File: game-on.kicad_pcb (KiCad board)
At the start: 2 copper layers, 125 x 70 mm, 339 parts, among them J1 USB_C, J2 Qwiic, J3 DEBUG, Q1 CJ2302, Q2 CJ2305, Q3 BC817, SW1 POWER, SW2 A, SW3 B, SW4 X, SW5 Y, SW6 RESET, SW7 BOOT, U1 HX9193-33GB, U2 QX2304, U3 ST7735S-SPI-14pin, U4 W25QXX128MBIT, U5 RP2040, X1 #badgelife, Y1 12MHz

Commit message: Tweaked a few values
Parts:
- C15, C16: value 15pF -> 30pF
- R13, R14: value 27 -> 27R
- R6: value 22R -> 27R
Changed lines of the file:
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@@
     (property "Sheetname" "Buttons")
     (attr through_hole)
-    (fp_text reference "SW2" (at 0 0.5 150) (layer "F.SilkS")
+    (fp_text reference "SW2" (at 0 0.5 150) (layer "F.SilkS") hide
       (effects (font (size 1 1) (thickness 0.15)))
     )
@@
     (property "Sheetname" "Buttons")
     (attr through_hole)
-    (fp_text reference "SW5" (at 0 0.5 60) (layer "F.SilkS")
+    (fp_text reference "SW5" (at 0 0.5 60) (layer "F.SilkS") hide
       (effects (font (size 1 1) (thickness 0.15)))
     )
@@
     (property "Sheetname" "Buttons")
     (attr through_hole)
-    (fp_text reference "SW3" (at 0 0.5 150) (layer "F.SilkS")
+    (fp_text reference "SW3" (at 0 0.5 150) (layer "F.SilkS") hide
       (effects (font (size 1 1) (thickness 0.15)))
     )
@@
     (property "Sheetname" "RP2040")
     (attr through_hole)
-    (fp_text reference "J3" (at 0 -2.33 90) (layer "F.SilkS")
+    (fp_text reference "J3" (at 0 -2.33 90) (layer "F.SilkS") hide
       (effects (font (size 1 1) (thickness 0.15)))
     )
@@
     (property "Sheetname" "Buttons")
     (attr through_hole)
-    (fp_text reference "SW4" (at 0 0.5 60) (layer "F.SilkS")
+    (fp_text reference "SW4" (at 0 0.5 60) (layer "F.SilkS") hide
       (effects (font (size 1 1) (thickness 0.15)))
     )
@@
       (net 1 "/PSU 2xAA/BAT+") (pinfunction "B") (pintype "passive"))
     (pad "3" smd rect (at 2.25 1.43 180) (size 0.7 1.5) (layers "B.Cu" "B.Paste" "B.Mask")
-      (net 57 "unconnected-(SW1-Pad3)") (pinfunction "C") (pintype "passive"))
+      (net 57 "unconnected-(SW1-Pad3)") (pinfunction "C") (pintype "passive+no_connect"))
     (model "${KICAD6_3DMODEL_DIR}/Button_Switch_SMD.3dshapes/SW_SPDT_PCM12.wrl"
       (offset (xyz 0 0 0))
@@
       (effects (font (size 1 1) (thickness 0.15)) (justify mirror))
     )
-    (fp_text value "15pF" (at 0 -1.43 135) (layer "B.Fab")
+    (fp_text value "30pF" (at 0 -1.43 135) (layer "B.Fab")
       (effects (font (size 1 1) (thickness 0.15)) (justify mirror))
     )
@@
       (effects (font (size 1 1) (thickness 0.15)) (justify mirror))
     )
-    (fp_text value "27" (at 0 -1.43 135) (layer "B.Fab")
+    (fp_text value "27R" (at 0 -1.43 135) (layer "B.Fab")
       (effects (font (size 1 1) (thickness 0.15)) (justify mirror))
     )
@@
       (effects (font (size 1 1) (thickness 0.15)) (justify mirror))
     )
-    (fp_text value "22R" (at 0 -1.43 45) (layer "B.Fab")
+    (fp_text value "27R" (at 0 -1.43 45) (layer "B.Fab")
       (effects (font (size 1 1) (thickness 0.15)) (justify mirror))
     )
@@
       (effects (font (size 1 1) (thickness 0.15)) (justify mirror))
     )
-    (fp_text value "15pF" (at 0 -1.43 135) (layer "B.Fab")
+    (fp_text value "30pF" (at 0 -1.43 135) (layer "B.Fab")
       (effects (font (size 1 1) (thickness 0.15)) (justify mirror))
     )
@@
       (effects (font (size 1 1) (thickness 0.15)) (justify mirror))
     )
-    (fp_text value "27" (at 0 -1.43 135) (layer "B.Fab")
+    (fp_text value "27R" (at 0 -1.43 135) (layer "B.Fab")
       (effects (font (size 1 1) (thickness 0.15)) (justify mirror))
     )

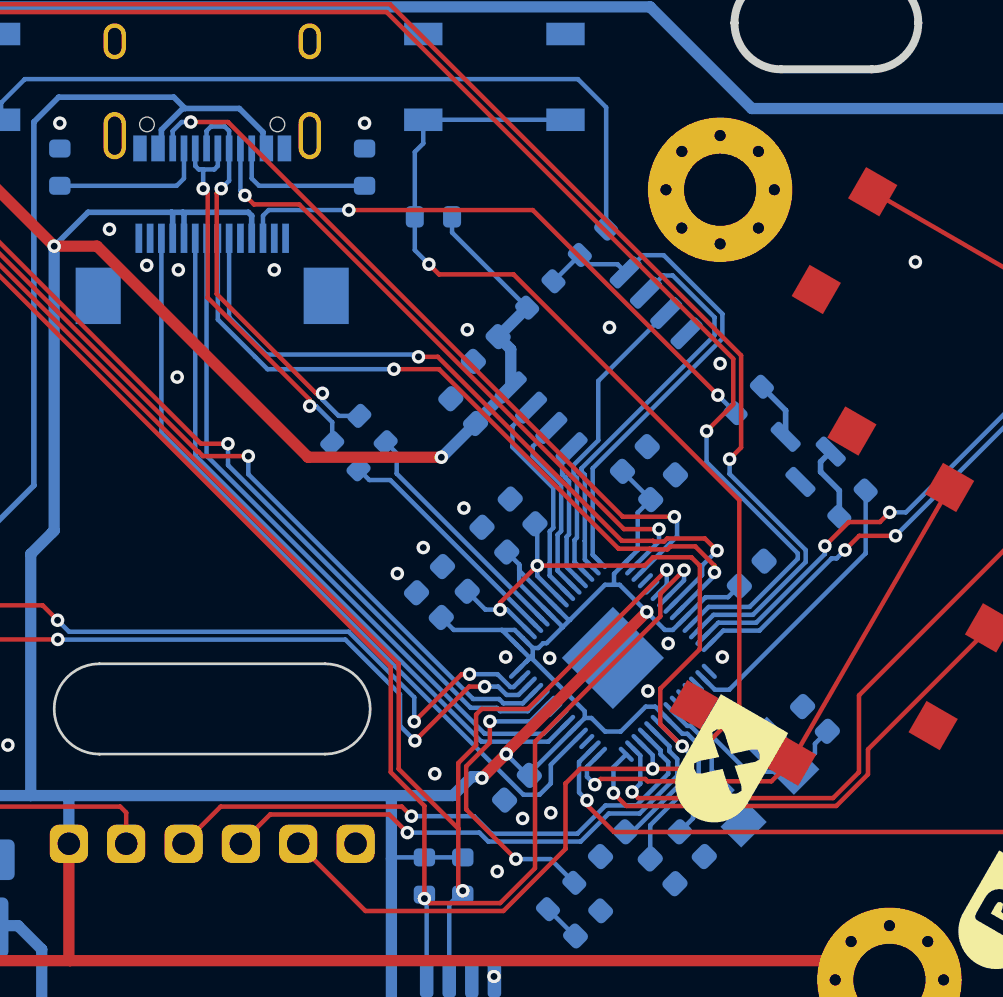
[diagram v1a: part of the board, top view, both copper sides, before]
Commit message: Adjusted fine pitch pads to allow matte black soldermask between
Also added a bit of silkscreen tweaks
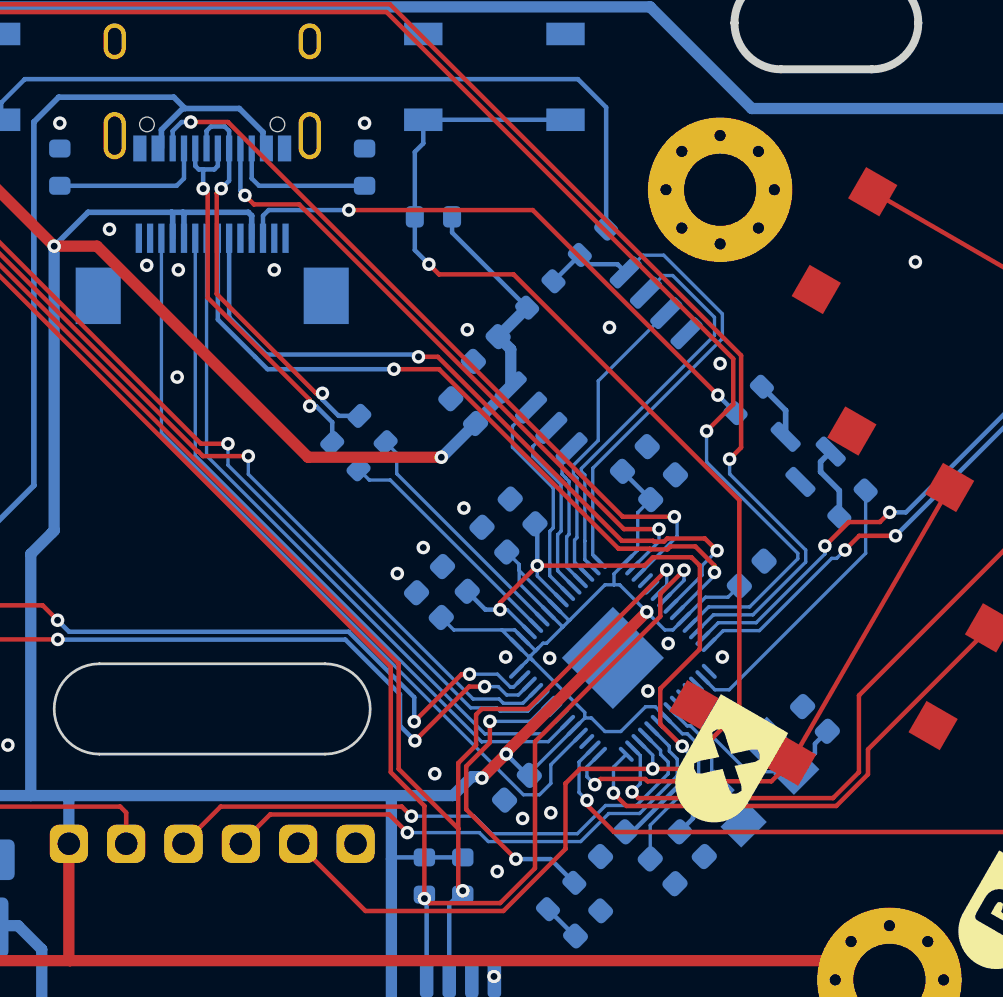
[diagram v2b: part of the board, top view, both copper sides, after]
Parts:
- added G***: LOGO, LOGO, B.Cu at (65.6, 73.1)
- added REF**: OSHW-Logo2_7.3x6mm_SilkScreen, Symbol:OSHW-Logo2_7.3x6mm_SilkScreen, B.Cu at (130.5, 91.6)
- added kibuzzard-62AC43D4: G***, kibuzzard-62AC43D4, B.Cu at (67.0, 69.4)
- added kibuzzard-62AC43F5: G***, kibuzzard-62AC43F5, B.Cu at (72.9, 61.5)
- added kibuzzard-62AC441C: G***, kibuzzard-62AC441C, B.Cu at (69.5, 64.0)
- added kibuzzard-62AC44E7: G***, kibuzzard-62AC44E7, B.Cu at (133.5, 69.4)
- added kibuzzard-62AC5196: G***, kibuzzard-62AC5196, B.Cu at (94.1, 62.8)
- moved kibuzzard-629FB487 2.83 mm to (76.5, 53.1)
- moved kibuzzard-629FB4BE 2.83 mm to (75.3, 56.4)
